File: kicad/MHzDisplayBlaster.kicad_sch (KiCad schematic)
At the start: 9 parts, among them J1 Conn_02x15 DigitLHS, J2 Conn_02x15 DigitRHS, J3 Conn_01x03_Pin, J4 Conn_01x02_Pin, U1 DC56-11GWA, U2 74LS04

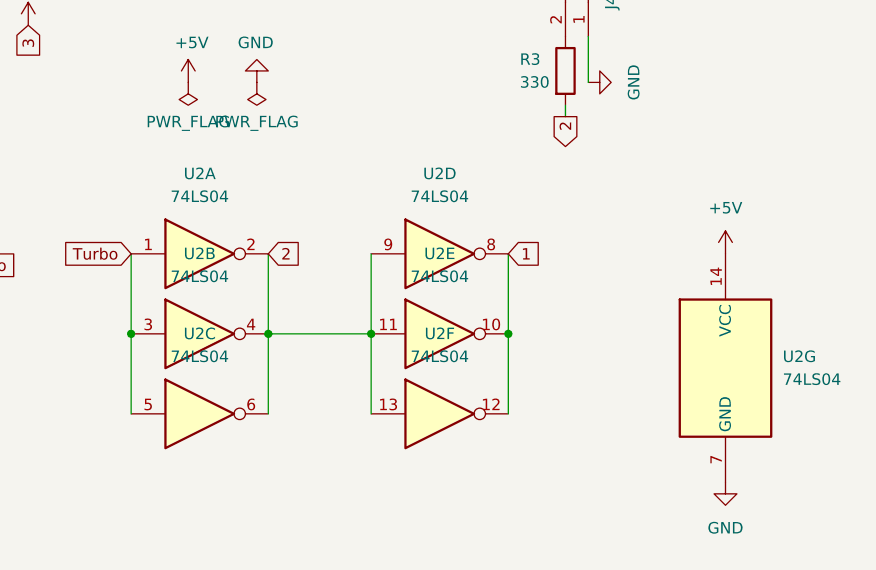
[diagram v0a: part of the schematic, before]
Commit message: Switch to 74HC04
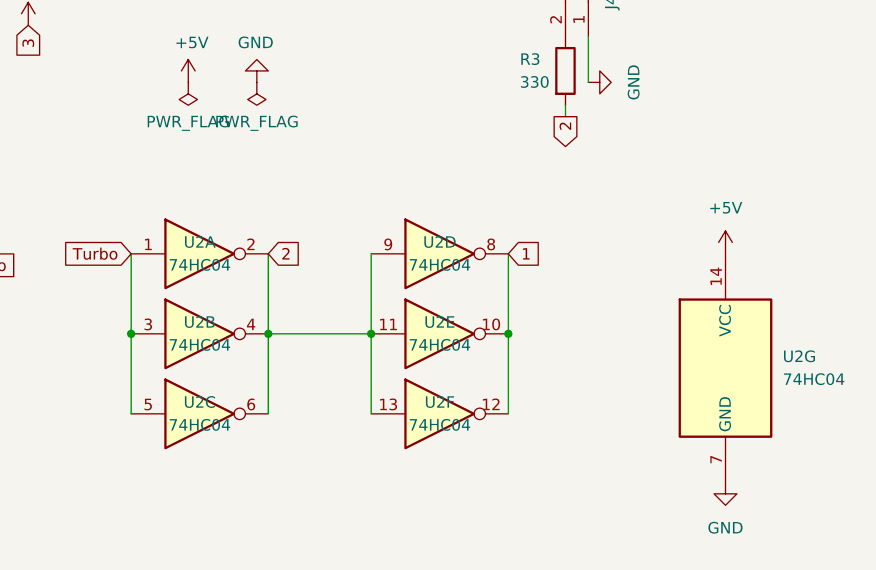
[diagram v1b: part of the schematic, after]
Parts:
- removed U2: 74LS04, Package_SO:SOIC-14_3.9x8.7mm_P1.27mm, symbol 74xx:74LS04
- added U2: 74HC04, Package_SO:SOIC-14_3.9x8.7mm_P1.27mm, symbol 74xx:74HC04
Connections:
- net +5V: now also U2.14 (VCC)
- net 1: now also U2.10, U2.12, U2.8
- net 2: now also U2.11, U2.13, U2.2, U2.4, U2.6, U2.9
- net GND: now also U2.7 (GND)
- net Turbo: now also U2.1, U2.3, U2.5

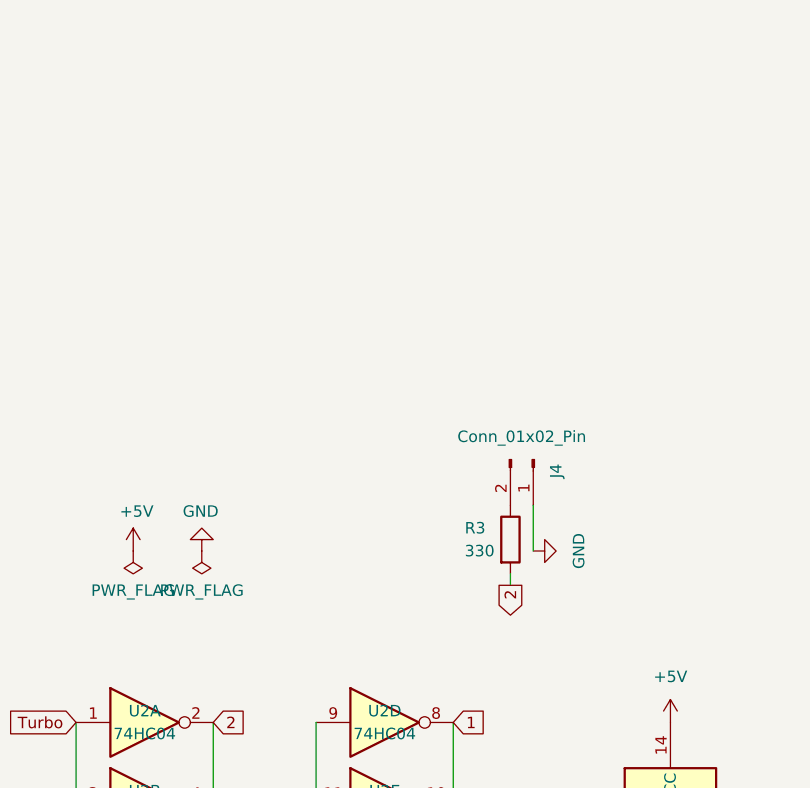
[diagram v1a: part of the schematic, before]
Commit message: Added 2N7000 MOSFET for LED header. KiCad 8
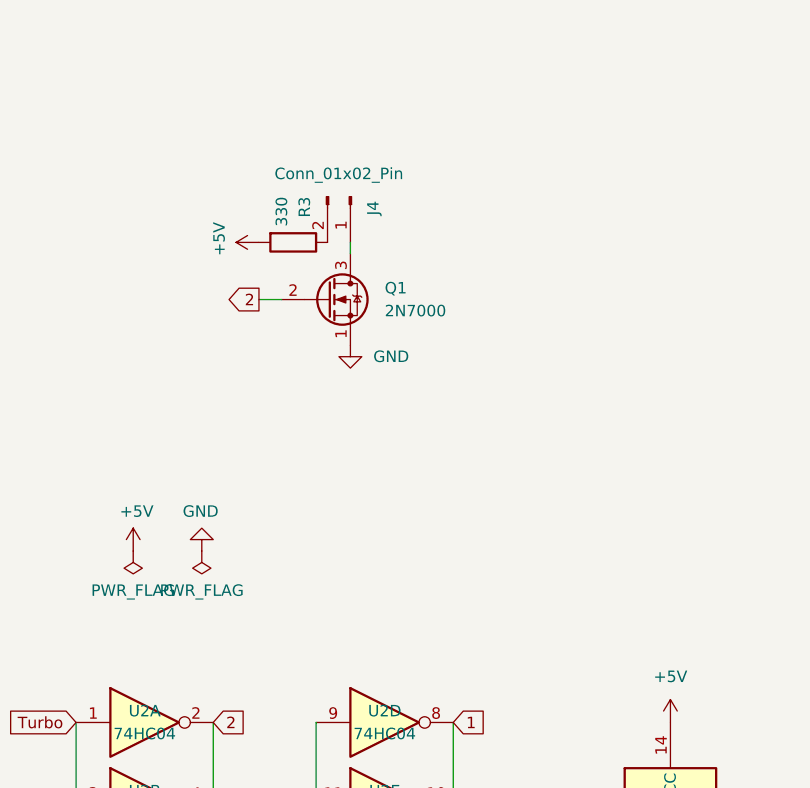
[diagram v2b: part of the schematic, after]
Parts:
- added Q1: 2N7000, Package_TO_SOT_THT:TO-92_Inline, symbol Transistor_FET:2N7000
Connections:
- net +5V: now also R3.2
- net 2: now also Q1.2 (G); no longer R3.2
- net GND: now also Q1.1 (S); no longer J4.1 (Pin_1)
- new net: J4.1 (Pin_1), Q1.3 (D)
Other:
- moved on the sheet: J4, R3

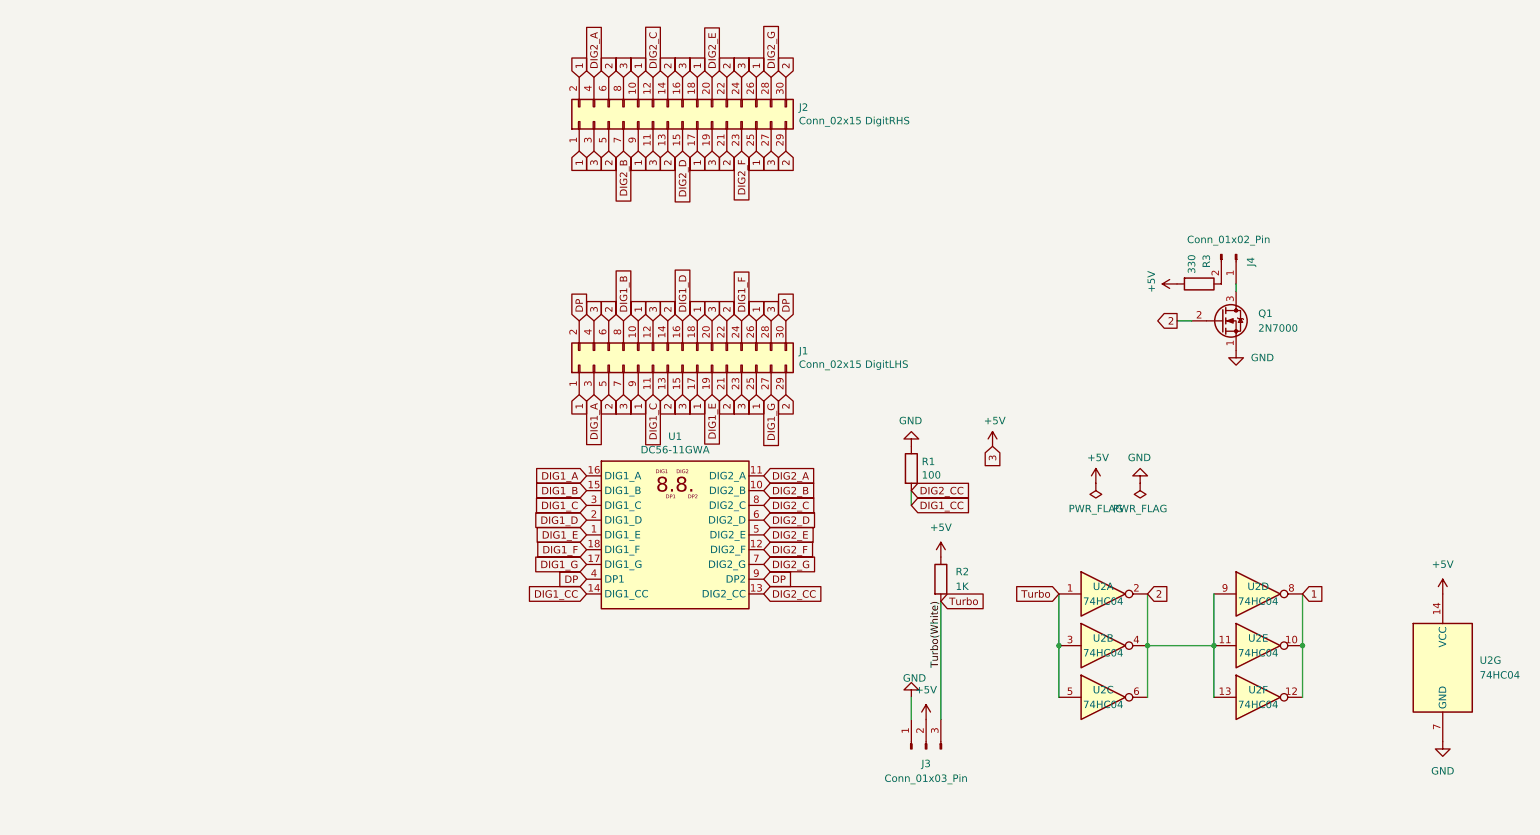
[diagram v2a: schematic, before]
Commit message: v1.2 - surface mount and better power management
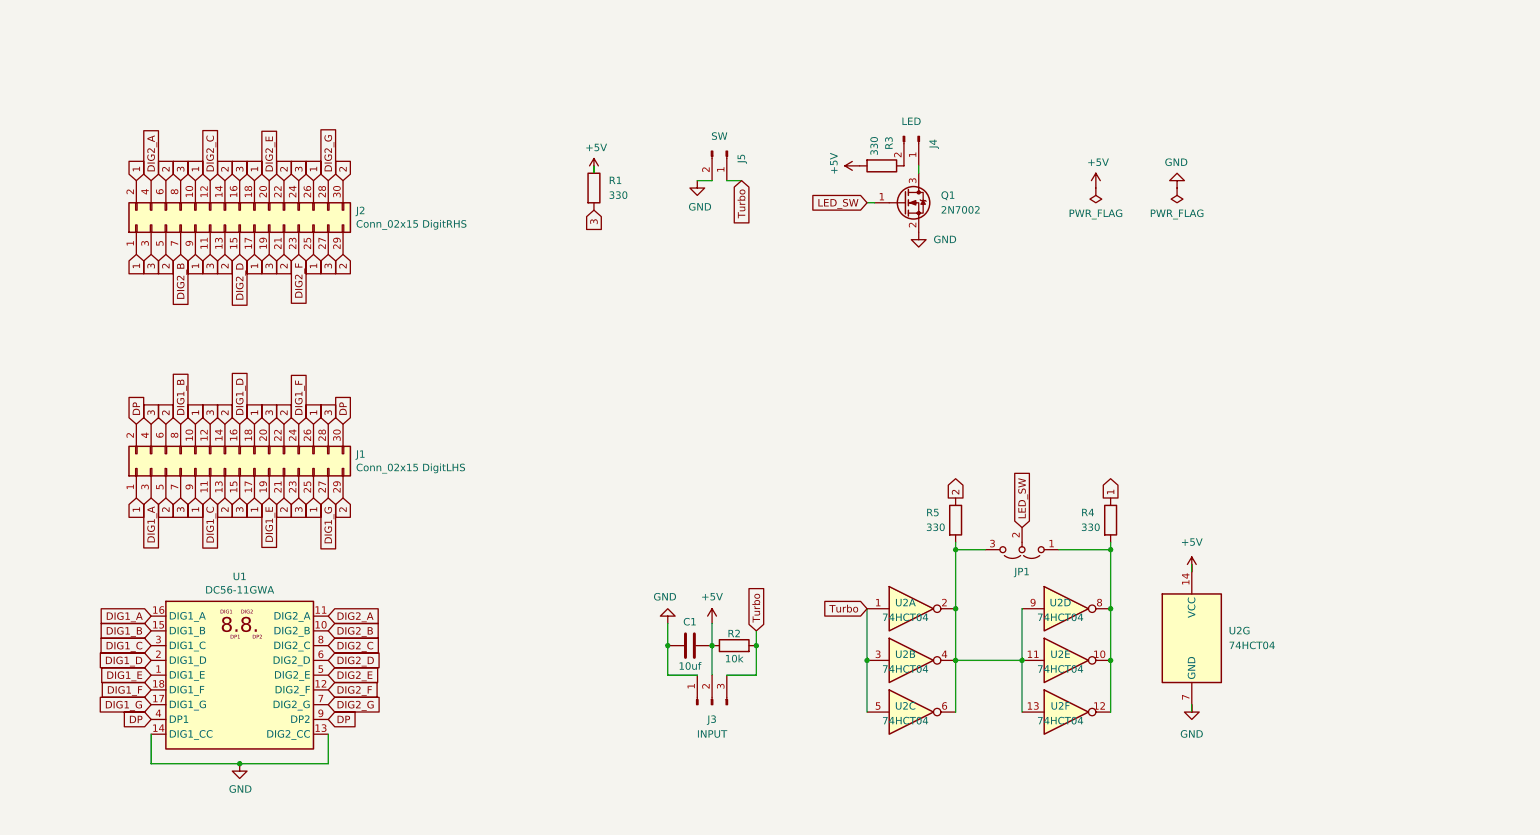
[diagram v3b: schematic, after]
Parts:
- removed Q1: 2N7000, Package_TO_SOT_THT:TO-92_Inline, symbol Transistor_FET:2N7000
- removed U2: 74HC04, Package_SO:SOIC-14_3.9x8.7mm_P1.27mm, symbol 74xx:74HC04
- added C1: 10uf, Capacitor_SMD:C_0805_2012Metric_Pad1.18x1.45mm_HandSolder, symbol Device:C
- added J5: SW, Connector_PinHeader_2.54mm:PinHeader_1x02_P2.54mm_Vertical, symbol Connector:Conn_01x02_Pin
- added JP1: Jumper_3_Open, Jumper:SolderJumper-3_P1.3mm_Open_RoundedPad1.0x1.5mm, symbol Jumper:Jumper_3_Open
- added Q1: 2N7002, Package_TO_SOT_SMD:SOT-23, symbol Transistor_FET:2N7002
- added R4, R5: 330, Resistor_SMD:R_0805_2012Metric_Pad1.20x1.40mm_HandSolder, symbol Device:R
- added U2: 74HCT04, Package_SO:SOIC-14_3.9x8.7mm_P1.27mm, symbol 74xx:74HCT04
- J3: value Conn_01x03_Pin -> INPUT
- J4: value Conn_01x02_Pin -> LED
- R1: value 100 -> 330; footprint Resistor_THT:R_Axial_DIN0204_L3.6mm_D1.6mm_P5.08mm_Horizontal -> Resistor_SMD:R_0805_2012Metric_Pad1.20x1.40mm_HandSolder
- R2: value 1K -> 10k; footprint Resistor_THT:R_Axial_DIN0204_L3.6mm_D1.6mm_P5.08mm_Horizontal -> Resistor_SMD:R_0805_2012Metric_Pad1.20x1.40mm_HandSolder
- R3: footprint Resistor_THT:R_Axial_DIN0204_L3.6mm_D1.6mm_P5.08mm_Horizontal -> Resistor_SMD:R_0805_2012Metric_Pad1.20x1.40mm_HandSolder
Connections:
- net +5V: now also R1.1, C1.2, U2.14 (VCC); no longer J1.12 (Pin_12), J1.15 (Pin_15), J1.20 (Pin_20), J1.23 (Pin_23), J1.28 (Pin_28), J1.4 (Pin_4), J1.7 (Pin_7), J2.11 (Pin_11), J2.16 (Pin_16), J2.19 (Pin_19), J2.24 (Pin_24), J2.27 (Pin_27), J2.3 (Pin_3), J2.8 (Pin_8)
- net 1: now also R4.1
- net 2: now also R5.1
- net GND: now also U1.13 (DIG2_CC), U1.14 (DIG1_CC), C1.1, J5.2 (Pin_2), Q1.2 (S), U2.7 (GND); no longer R1.1
- net Turbo: now also J5.1 (Pin_1), U2.1, U2.3, U2.5
- net at J4.1 (Pin_1): now also Q1.3 (D)
- removed net DIG1_CC: R1.2, U1.13 (DIG2_CC), U1.14 (DIG1_CC)
- new net: JP1.1 (A), R4.2, U2.10, U2.12, U2.8
- new net: JP1.3 (B), R5.2, U2.11, U2.13, U2.2, U2.4, U2.6, U2.9
- new net 3: J1.12 (Pin_12), J1.15 (Pin_15), J1.20 (Pin_20), J1.23 (Pin_23), J1.28 (Pin_28), J1.4 (Pin_4), J1.7 (Pin_7), J2.11 (Pin_11), J2.16 (Pin_16), J2.19 (Pin_19), J2.24 (Pin_24), J2.27 (Pin_27), J2.3 (Pin_3), J2.8 (Pin_8), R1.2
- new net LED_SW: JP1.2 (C), Q1.1 (G)
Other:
- moved on the sheet: J1, J2, J3, J4, R2, R3, U1

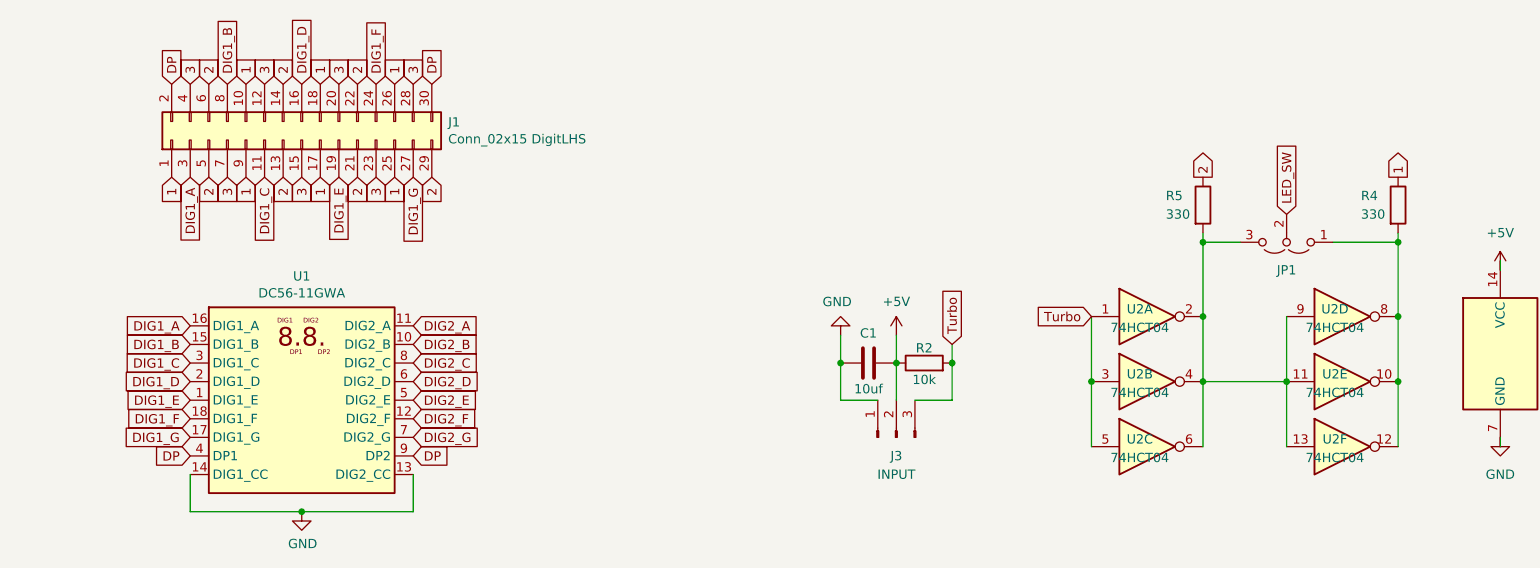
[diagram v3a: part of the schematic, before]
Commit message: Added Individual segment resistors
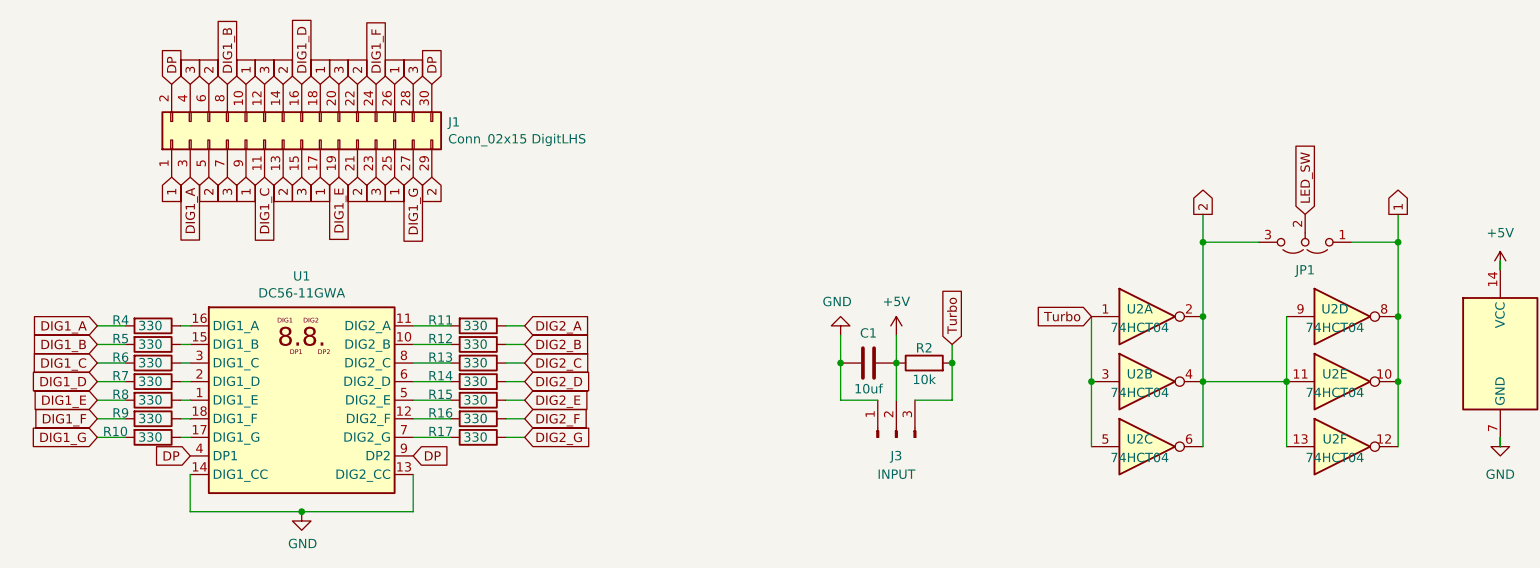
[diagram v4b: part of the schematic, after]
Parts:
- added R10, R11, R12, R13, R14, R15, R16, R17, R6, R7, R8, R9: 330, Resistor_SMD:R_0805_2012Metric_Pad1.20x1.40mm_HandSolder, symbol Device:R
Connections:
- net 1: now also JP1.1 (A), U2.10, U2.12, U2.8; no longer R4.1
- net 2: now also JP1.3 (B), U2.11, U2.13, U2.2, U2.4, U2.6, U2.9; no longer R5.1
- net DIG1_A: now also R4.2; no longer U1.16 (DIG1_A)
- net DIG1_B: now also R5.2; no longer U1.15 (DIG1_B)
- net DIG1_C: now also R6.2; no longer U1.3 (DIG1_C)
- net DIG1_D: now also R7.2; no longer U1.2 (DIG1_D)
- net DIG1_E: now also R8.2; no longer U1.1 (DIG1_E)
- net DIG1_F: now also R9.2; no longer U1.18 (DIG1_F)
- net DIG1_G: now also R10.2; no longer U1.17 (DIG1_G)
- net DIG2_A: now also R11.1; no longer U1.11 (DIG2_A)
- net DIG2_B: now also R12.1; no longer U1.10 (DIG2_B)
- net DIG2_C: now also R13.1; no longer U1.8 (DIG2_C)
- net DIG2_D: now also R14.1; no longer U1.6 (DIG2_D)
- net DIG2_E: now also R15.1; no longer U1.5 (DIG2_E)
- net DIG2_F: now also R16.1; no longer U1.12 (DIG2_F)
- net DIG2_G: now also R17.1; no longer U1.7 (DIG2_G)
- new net: R8.1, U1.1 (DIG1_E)
- new net: R12.2, U1.10 (DIG2_B)
- new net: R11.2, U1.11 (DIG2_A)
- new net: R16.2, U1.12 (DIG2_F)
- new net: R5.1, U1.15 (DIG1_B)
- new net: R4.1, U1.16 (DIG1_A)
- new net: R10.1, U1.17 (DIG1_G)
- new net: R9.1, U1.18 (DIG1_F)
- new net: R7.1, U1.2 (DIG1_D)
- new net: R6.1, U1.3 (DIG1_C)
- new net: R15.2, U1.5 (DIG2_E)
- new net: R14.2, U1.6 (DIG2_D)
- new net: R17.2, U1.7 (DIG2_G)
- new net: R13.2, U1.8 (DIG2_C)
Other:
- moved on the sheet: JP1, R4
